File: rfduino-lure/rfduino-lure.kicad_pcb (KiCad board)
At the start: 2 copper layers, 54.6 x 50.8 mm, 4 parts, among them U1 RFDUINO_SHEILD, U2 MAX_LSE, U3 RFDUINO_IO

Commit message: some refactoring
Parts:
- removed U3: RFDUINO_IO, SIL-8
- added RFDUINO_SHEILD (x7): VAL**, RFDUINO_SHEILD, F.Cu at (0.00, 0.00)
- added USB1: USB-PROGRAMMER, SIL-6, F.Cu at (190.5, 162.6)
- U1: value RFDUINO_SHEILD -> RFDUINO_IO; footprint pin_array_6x2 -> SIL-8
- moved U1 13.3 mm to (193.0, 142.2), turned to 180 degrees
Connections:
- BLE1 pad 1: N-0000013 -> N-0000011
- BLE1 pad 2: N-0000014 -> N-0000012
- BLE1 pad 8: N-000001 (its old number) -> N-0000010
- U1 pad 1: (no net) -> N-0000011
- U1 pad 2: (no net) -> N-0000012
- U1 pad 8: (no net) -> N-0000010
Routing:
- net N-000001: track 0.00 -> 34.2 mm, vias 0 -> 2
- net N-000002: track 0.00 -> 33.7 mm, vias 0 -> 2
- net N-0000010: track 0.00 -> 31.0 mm
- net N-0000016: track 17.2 -> 46.2 mm, vias 0 -> 2
- net N-000001 (its old number): track 27.9 -> 0.00 mm
- net N-0000018: track 17.7 -> 44.2 mm, vias 0 -> 2
- net N-000009: track 59.3 -> 36.1 mm, vias 2 -> 0
- net N-000008: track 29.8 -> 52.2 mm, vias 2 -> 3
- net N-000007: track 31.5 -> 50.9 mm
- net N-000004: track 28.0 -> 43.3 mm, vias 0 -> 2
- net N-0000014: track 13.1 -> 0.00 mm, vias 2 -> 0
- net N-0000013: track 11.1 -> 0.00 mm
- net N-000003: track 49.4 -> 39.8 mm, vias 3 -> 2
- net N-0000011: track 0.00 -> 4.19 mm, vias 0 -> 2
- net N-0000012: track 0.00 -> 2.18 mm, vias 0 -> 1
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- added copper zone on B.Cu, net N-0000011
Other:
- board text added: "+3v"
- board text added: "GND"

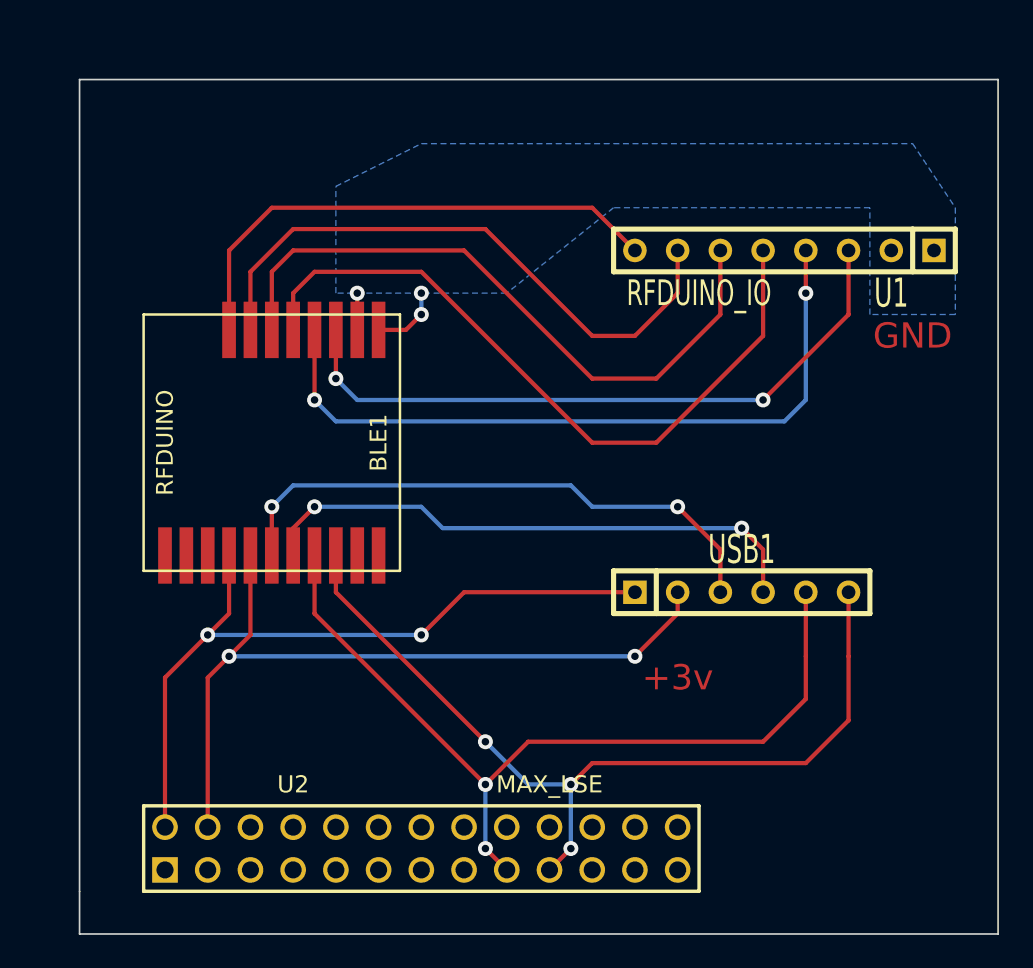
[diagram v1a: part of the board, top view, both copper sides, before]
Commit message: added ground plane
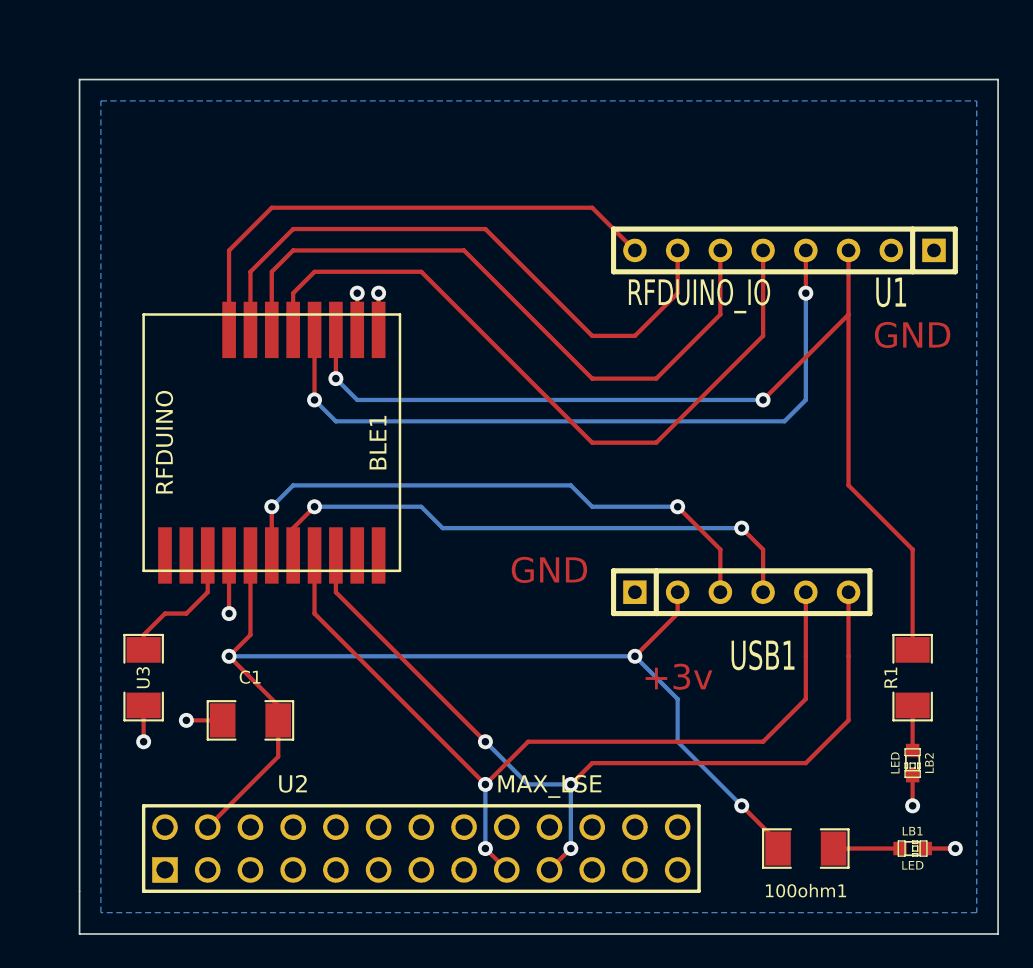
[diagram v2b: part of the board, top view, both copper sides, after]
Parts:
- added 100ohm1: R, SM1206, F.Cu at (194.3, 177.8)
- added C1: 100nf, SM1206, F.Cu at (161.3, 170.2)
- added LB1: LED, LED-0603, F.Cu at (200.7, 177.8)
- added LB2: LED, LED-0603, F.Cu at (200.7, 172.7)
- added R1: 100ohm, SM1206, F.Cu at (200.7, 167.6)
- added U3: EXT_ANT, SM1206, F.Cu at (154.9, 167.6)
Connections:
- BLE1 pad 1: N-0000011 -> N-0000031
- BLE1 pad 11: (no net) -> N-000009
- BLE1 pad 12: N-0000018 -> N-0000031
- BLE1 pad 2: N-0000012 -> N-0000031
- U1 pad 1: N-0000011 -> N-0000031
- U1 pad 2: N-0000012 -> N-0000031
- U2 pad 2: N-0000018 -> N-0000031
- USB1 pad 1: N-0000018 -> N-0000031
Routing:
- net N-0000018: track 44.2 -> 0.00 mm, vias 2 -> 0
- net N-0000010: track 39.8 -> 61.3 mm
- net N-0000032: track 46.2 -> 63.6 mm, vias 2 -> 3
- net N-0000031: track 0.00 -> 15.7 mm, vias 0 -> 7
- net N-000009: track 0.00 -> 7.94 mm
- net N-000008: track 0.00 -> 3.95 mm
- net N-0000012: track 2.18 -> 0.00 mm, vias 1 -> 0
- net N-0000011: track 4.19 -> 2.68 mm, vias 2 -> 0
- added copper zone on B.Cu, net N-0000031
- removed copper zone on B.Cu, net N-0000011
